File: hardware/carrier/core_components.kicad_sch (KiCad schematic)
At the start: 54 parts, among them J1 PANEL, J2 CARDKB, J3 HAPTIC, J4 EXT_LED, J5 PIEZ, M1 Walter, Q1 UMH3N, Q2 SI1308EDL, Q3 MMST3904, SW1 SKQGAFE010, U1 CP2102N-A02-GQFN24, U2 SN74LVC2G126DCUR, U3 DRV2605LDGSR, U4 LIS2DW12TR

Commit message: Replace JP1 with 0402 0R link, shrink SW1/SW2 to KMR2 and MSK12C02
JP1 (solder jumper) becomes R39, a fitted 0402 0R on the auto-boot line:
pull it to disable auto boot. SW1 is now a C&K KMR221GLFS (4.2 x 2.8 x
1.3 mm, C72443) and SW2 a Shou Han MSK12C02 top-knob slide switch
(C431540). Footprints swapped in the PCB with nets preserved (SW1 pads
now carry FL_BTN/GND). Adds the JLCPCB design rules file.

Co-Authored-By: Claude Fable 5.1 <noreply@anthropic.com>
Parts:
- R39: renamed from JP1; value auto-boot -> 0R; footprint Jumper:SolderJumper-2_P1.3mm_Bridged_RoundedPad1.0x1.5mm -> Resistor_SMD:R_0402_1005Metric; symbol Jumper:SolderJumper_2_Bridged -> Device:R; LCSC (none) -> C17168; MPN (none) -> 0402WGF0000TCE; Note open to disable auto boot mode -> auto-boot link: remove to disable auto boot mode
- SW1: value SKQGAFE010 -> KMR221GLFS; footprint Button_Switch_SMD:SW_SPST_SKQG_WithoutStem -> Button_Switch_SMD:SW_Push_1P1T_NO_CK_KMR2; LCSC C202424 -> C72443; MPN SKQGAFE010 -> KMR221GLFS; Note Alps 5.2 x 5.2 x 1.5 mm, 1 N, top actuated -> C&K KMR2 4.2 x 2.8 x 1.3 mm, 2 N, top actuated
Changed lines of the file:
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@@
 	(wire
 		(pts
+			(xy 175.26 243.84) (xy 176.53 243.84)
+		)
+		(stroke
+			(width 0)
+			(type default)
+		)
+	)
+	(wire
+		(pts
+			(xy 184.15 243.84) (xy 185.42 243.84)
+		)
+		(stroke
+			(width 0)
+			(type default)
+		)
+	)
+	(wire
+		(pts
 			(xy 147.32 203.2) (xy 147.32 210.82)
 		)
@@
 	)
 	(symbol
-		(lib_id "Jumper:SolderJumper_2_Bridged")
-		(at 180.34 243.84 0)
+		(lib_id "Device:R")
+		(at 180.34 243.84 90)
 		(unit 1)
 		(body_style 1)
@@
 		(in_pos_files yes)
 		(dnp no)
-		(property "Reference" "JP1"
+		(property "Reference" "R39"
 			(at 179.07 246.634 0)
 			(show_name no)
@@
 			)
 		)
-		(property "Value" "auto-boot"
+		(property "Value" "0R"
 			(at 178.816 248.666 0)
 			(show_name no)
@@
 			)
 		)
-		(property "Footprint" "Jumper:SolderJumper-2_P1.3mm_Bridged_RoundedPad1.0x1.5mm"
+		(property "Footprint" "Resistor_SMD:R_0402_1005Metric"
 			(at 186.69 247.65 0)
 			(hide yes)
@@
 			)
 		)
-		(property "Description" "Solder Jumper, 2-pole, closed/bridged"
+		(property "Description" "Resistor"
 			(at 186.69 252.73 0)
 			(hide yes)
@@
 			)
 		)
-		(property "MPN" ""
+		(property "MPN" "0402WGF0000TCE"
 			(at 180.34 259.08 0)
 			(hide yes)
@@
 			)
 		)
-		(property "LCSC" ""
+		(property "LCSC" "C17168"
 			(at 180.34 261.62 0)
 			(hide yes)
@@
 			)
 		)
-		(property "Note" "open to disable auto boot mode"
+		(property "Note" "auto-boot link: remove to disable auto boot mode"
 			(at 180.34 266.7 0)
 			(hide yes)
@@
 			(project "pager-carrier"
 				(path "/4c77a02c-35a9-4533-b036-187d3e0c67ce"
-					(reference "JP1")
+					(reference "R39")
 					(unit 1)
 				)
@@
 			)
 		)
-		(property "Value" "SKQGAFE010"
+		(property "Value" "KMR221GLFS"
 			(at 99.822 110.998 90)
 			(show_name no)
@@
 			)
 		)
-		(property "Footprint" "Button_Switch_SMD:SW_SPST_SKQG_WithoutStem"
+		(property "Footprint" "Button_Switch_SMD:SW_Push_1P1T_NO_CK_KMR2"
 			(at 107.95 115.57 0)
 			(hide yes)
@@
 			)
 		)
-		(property "MPN" "SKQGAFE010"
+		(property "MPN" "KMR221GLFS"
 			(at 119.38 109.22 0)
 			(hide yes)
@@
 			)
 		)
-		(property "LCSC" "C202424"
+		(property "LCSC" "C72443"
 			(at 121.92 109.22 0)
 			(hide yes)
@@
 			)
 		)
-		(property "Note" "Alps 5.2 x 5.2 x 1.5 mm, 1 N, top actuated"
+		(property "Note" "C&K KMR2 4.2 x 2.8 x 1.3 mm, 2 N, top actuated"
 			(at 127 109.22 0)
 			(hide yes)

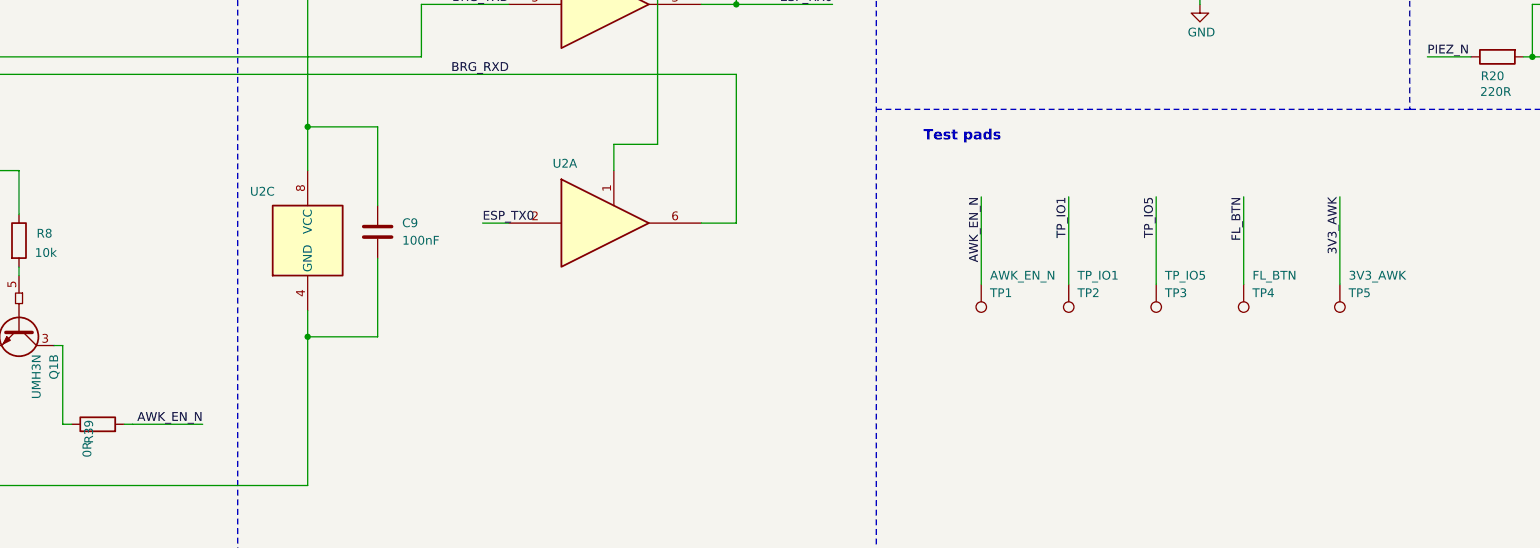
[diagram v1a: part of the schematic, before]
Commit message: Carrier schematics: owner's updates to core and power sheets
Owner edits made in KiCad alongside the v0.2c layout work (library symbol
and sheet changes in core_components and power_components).

Co-Authored-By: Claude Fable 5.1 <noreply@anthropic.com>
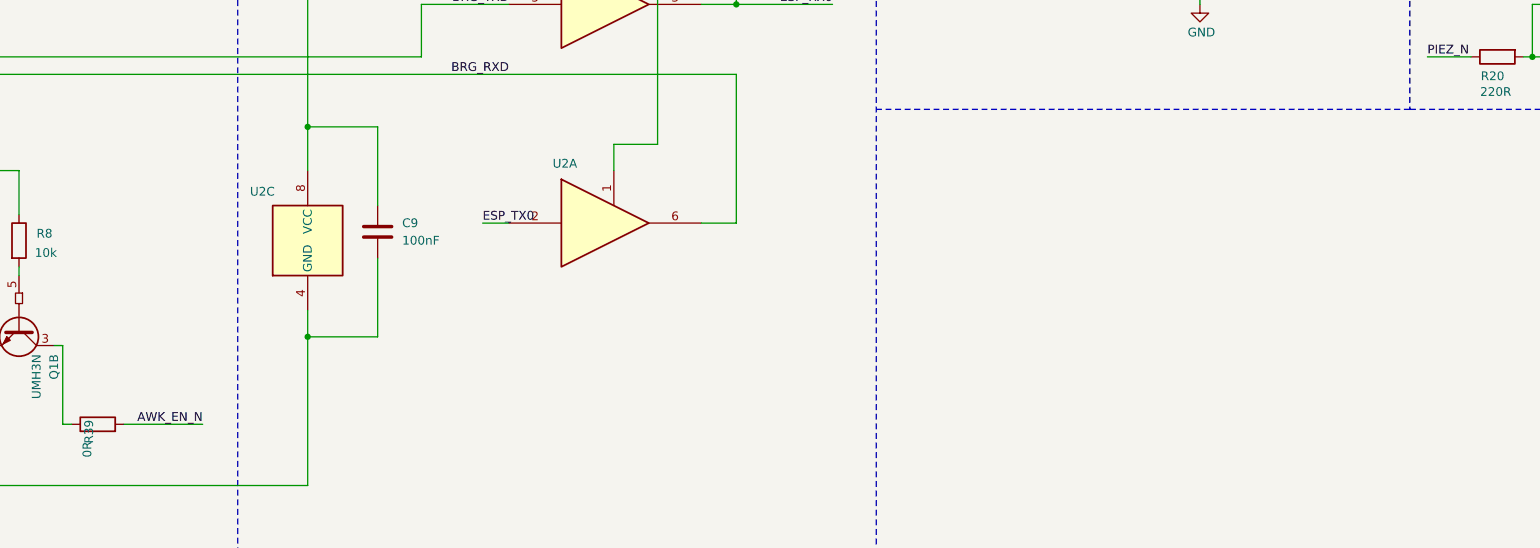
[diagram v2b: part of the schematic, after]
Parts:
- removed TP1: AWK_EN_N, TestPoint:TestPoint_Pad_1.0x1.0mm, symbol Connector:TestPoint
- removed TP2: TP_IO1, TestPoint:TestPoint_Pad_1.0x1.0mm, symbol Connector:TestPoint
- removed TP3: TP_IO5, TestPoint:TestPoint_Pad_1.0x1.0mm, symbol Connector:TestPoint
- removed TP4: FL_BTN, TestPoint:TestPoint_Pad_1.0x1.0mm, symbol Connector:TestPoint
- removed TP5: 3V3_AWK, TestPoint:TestPoint_Pad_1.0x1.0mm, symbol Connector:TestPoint
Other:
- note removed: "Test pads"

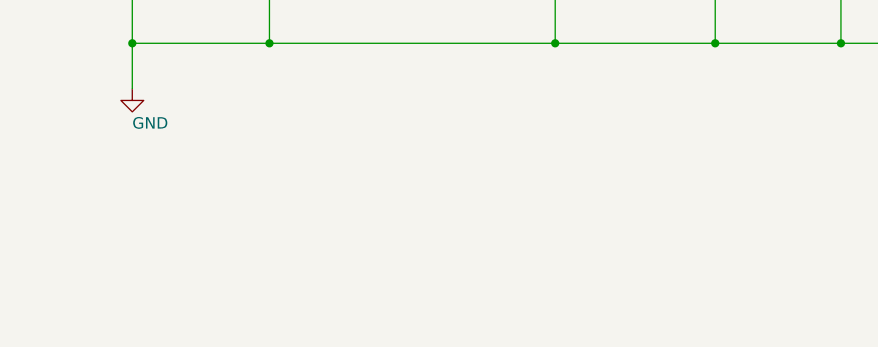
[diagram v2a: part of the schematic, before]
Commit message: Carrier v0.2c WIP: cassette screw holes, top-actuated SW2, wider board, panel schematic fixes
Work in progress for the 3D-printed display cassette; routing is DRC-clean
(0 errors) with 14 signal links and 3 ground islands left for hand finishing
(list in HANDOFF-v0.2.md).

Carrier:
- H1-H3 M2 cassette screw holes (2.2 mm NPTH, 4.5 mm copper-free annulus on
  both layers via footprint rule areas + per-hole DRC rules) at (77.4, 60.9),
  (111.2, 59.95), (111.2, 105.85); schematic symbols in the core sheet.
- SW2 power switch -> C&K JS102011SAQN top-actuated SPDT (LCSC C221660),
  travel along X; top strip is now J6, SW1, SW2 (x 80.0..108.5).
- Board widened to x 120.5 so the right-side holes fit beside the header
  column (J2 keyboard header stays topmost, cable into the plate channel).
- F.Fab note to trim the Walter header pins flush; stale KBD label moved.
- 3D models added: JS102011SAQN, MAX17048 (U6), JST PH S2B-PH-SM4-TB (J7);
  STEP export in out/ for the Fusion assembly.
- Owner's manual schematic edits (test points) included.

Panel:
- Owner's rearranged panel_main.kicad_sch with the EPD_GDR wire gap closed
  (J1 pin 2 back on the boost gate net); both front-light FPC connectors kept.

Co-Authored-By: Claude Fable 5.1 <noreply@anthropic.com>
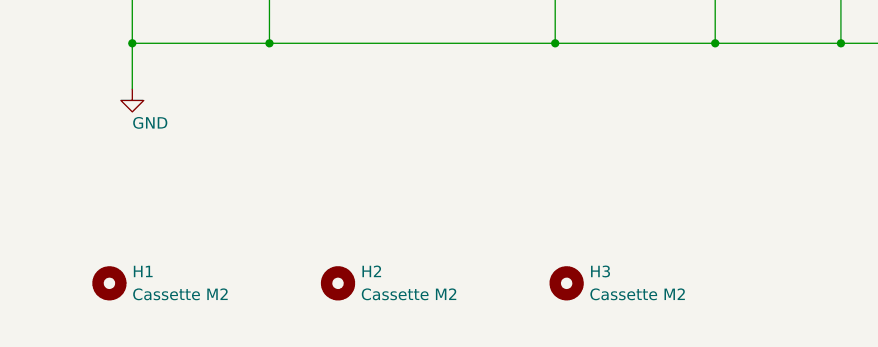
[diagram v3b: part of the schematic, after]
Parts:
- added H1, H2, H3: Cassette M2, pager-carrier:MountingHole_2.2mm_M2_Cassette, symbol Mechanical:MountingHole
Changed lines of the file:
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@@
 	)
 	(embedded_fonts no)
+	(symbol
+		(lib_id "Mechanical:MountingHole")
+		(at 25.4 279.4 0)
+		(unit 1)
+		(exclude_from_sim no)
+		(in_bom no)
+		(on_board yes)
+		(dnp no)
+		(property "Reference" "H1"
+			(at 27.939999999999998 278.13 0)
+			(effects (font (size 1.27 1.27)) (justify left))
+		)
+		(property "Value" "Cassette M2"
+			(at 27.939999999999998 280.66999999999996 0)
+			(effects (font (size 1.27 1.27)) (justify left))
+		)
+		(property "Footprint" "pager-carrier:MountingHole_2.2mm_M2_Cassette"
+			(at 25.4 279.4 0)
+			(effects (font (size 1.27 1.27)) (hide yes))
+		)
+		(property "Datasheet" ""
+			(at 25.4 279.4 0)
+			(effects (font (size 1.27 1.27)) (hide yes))
+		)
+		(property "Description" "Display cassette standoff screw hole, 2.2 mm NPTH, 4.5 mm copper-free annulus"
+			(at 25.4 279.4 0)
+			(effects (font (size 1.27 1.27)) (hide yes))
+		)
+		(instances
+			(project "pager-carrier"
+				(path "/ab8ee99e-0f89-4d3d-ba18-cf2cd7eb7e8f"
+					(reference "H1")
+					(unit 1)
+				)
+			)
+		)
+	)
+	(symbol
+		(lib_id "Mechanical:MountingHole")
+		(at 50.8 279.4 0)
+		(unit 1)
+		(exclude_from_sim no)
+		(in_bom no)
+		(on_board yes)
+		(dnp no)
+		(property "Reference" "H2"
+			(at 53.339999999999996 278.13 0)
+			(effects (font (size 1.27 1.27)) (justify left))
+		)
+		(property "Value" "Cassette M2"
+			(at 53.339999999999996 280.66999999999996 0)
+			(effects (font (size 1.27 1.27)) (justify left))
+		)
+		(property "Footprint" "pager-carrier:MountingHole_2.2mm_M2_Cassette"
+			(at 50.8 279.4 0)
+			(effects (font (size 1.27 1.27)) (hide yes))
+		)
+		(property "Datasheet" ""
+			(at 50.8 279.4 0)
+			(effects (font (size 1.27 1.27)) (hide yes))
+		)
+		(property "Description" "Display cassette standoff screw hole, 2.2 mm NPTH, 4.5 mm copper-free annulus"
+			(at 50.8 279.4 0)
+			(effects (font (size 1.27 1.27)) (hide yes))
+		)
+		(instances
+			(project "pager-carrier"
+				(path "/ab8ee99e-0f89-4d3d-ba18-cf2cd7eb7e8f"
+					(reference "H2")
+					(unit 1)
+				)
+			)
+		)
+	)
+	(symbol
+		(lib_id "Mechanical:MountingHole")
+		(at 76.19999999999999 279.4 0)
+		(unit 1)
+		(exclude_from_sim no)
+		(in_bom no)
+		(on_board yes)
+		(dnp no)
+		(property "Reference" "H3"
+			(at 78.74 278.13 0)
+			(effects (font (size 1.27 1.27)) (justify left))
+		)
+		(property "Value" "Cassette M2"
+			(at 78.74 280.66999999999996 0)
+			(effects (font (size 1.27 1.27)) (justify left))
+		)
+		(property "Footprint" "pager-carrier:MountingHole_2.2mm_M2_Cassette"
+			(at 76.19999999999999 279.4 0)
+			(effects (font (size 1.27 1.27)) (hide yes))
+		)
+		(property "Datasheet" ""
+			(at 76.19999999999999 279.4 0)
+			(effects (font (size 1.27 1.27)) (hide yes))
+		)
+		(property "Description" "Display cassette standoff screw hole, 2.2 mm NPTH, 4.5 mm copper-free annulus"
+			(at 76.19999999999999 279.4 0)
+			(effects (font (size 1.27 1.27)) (hide yes))
+		)
+		(instances
+			(project "pager-carrier"
+				(path "/ab8ee99e-0f89-4d3d-ba18-cf2cd7eb7e8f"
+					(reference "H3")
+					(unit 1)
+				)
+			)
+		)
+	)
 )
